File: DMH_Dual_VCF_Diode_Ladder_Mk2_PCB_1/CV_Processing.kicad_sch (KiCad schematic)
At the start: 45 parts, among them SW10 SW_DPDT_OnOn, SW7 SW_SPDT_OnOffOn, SW9 SW_SPDT_OnOffOn, U5 TL074, U6 TL074, U7 TL074

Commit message: Added CV3 and Drive CV to I/O pages
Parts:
- SW7, SW9: Function Bus CV Amt -> CV 3 Amt
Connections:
- net Bus CV A Input renamed CV3 A Input
- net Bus CV B Input renamed CV3 B Input
- net Link Switch renamed Link CV Switch
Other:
- moved on the sheet: D3, D4, D5, R11, R12, R13, R14, R15, RV6, SW10

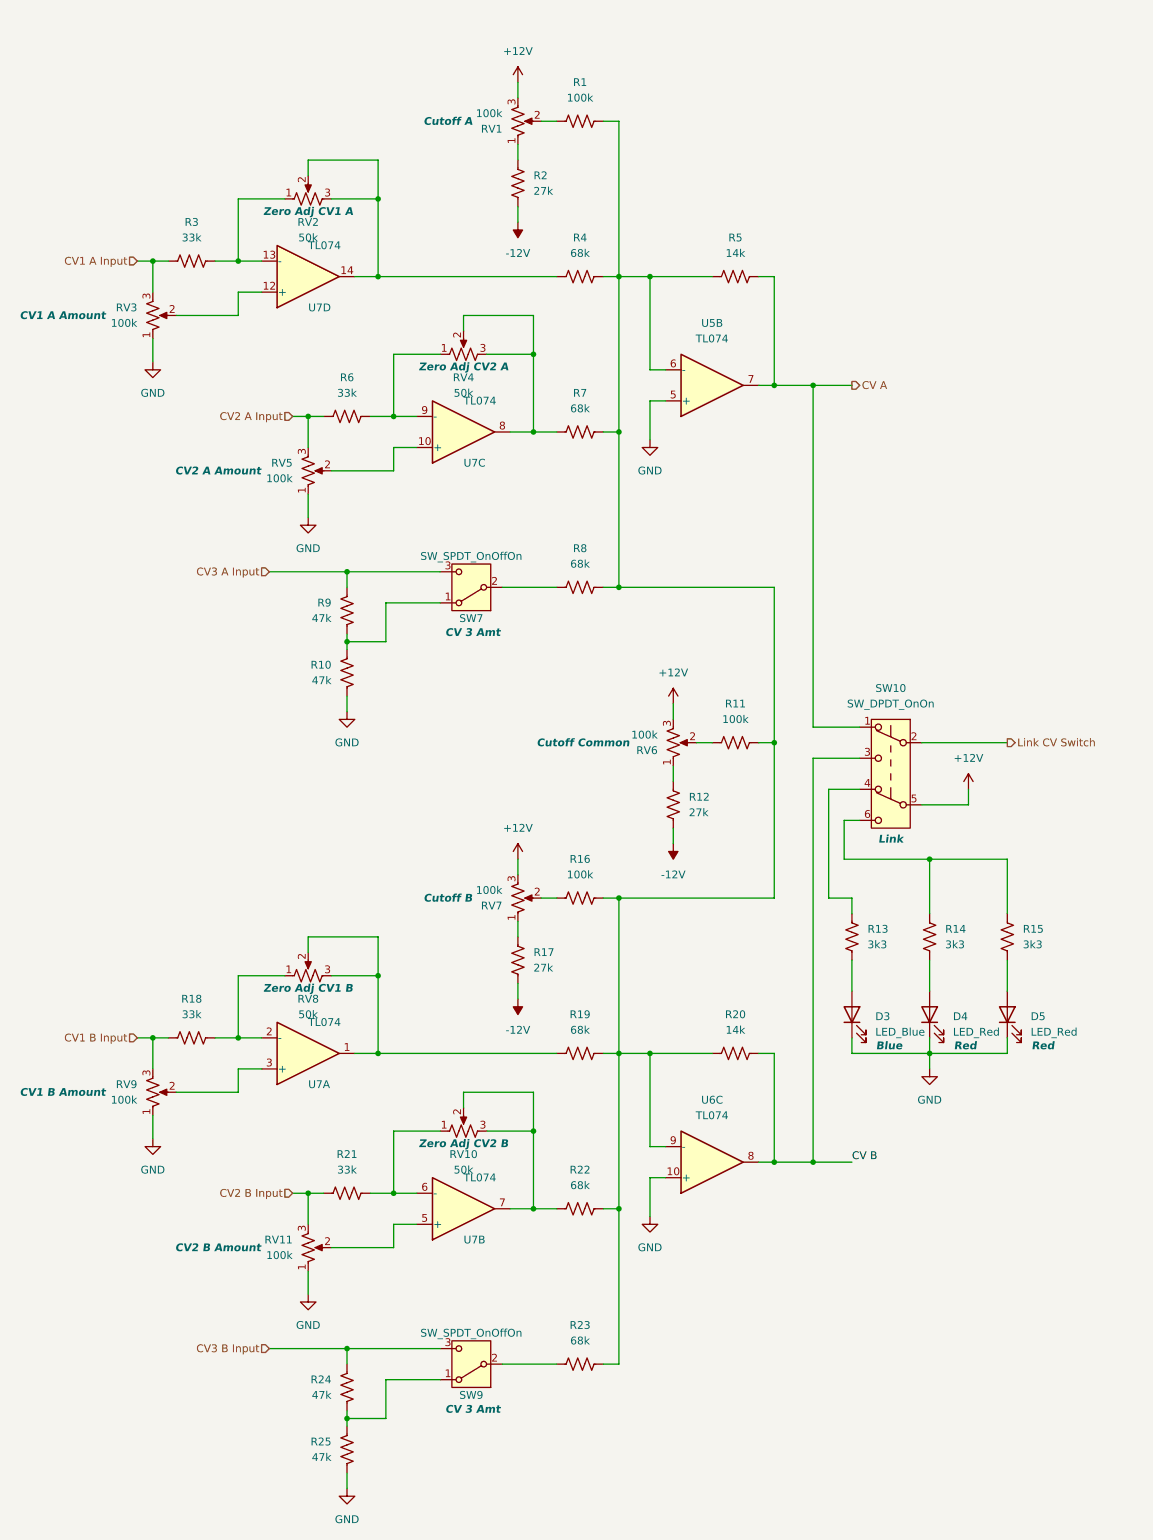
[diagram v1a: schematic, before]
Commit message: Added board-to-board pins to schematic
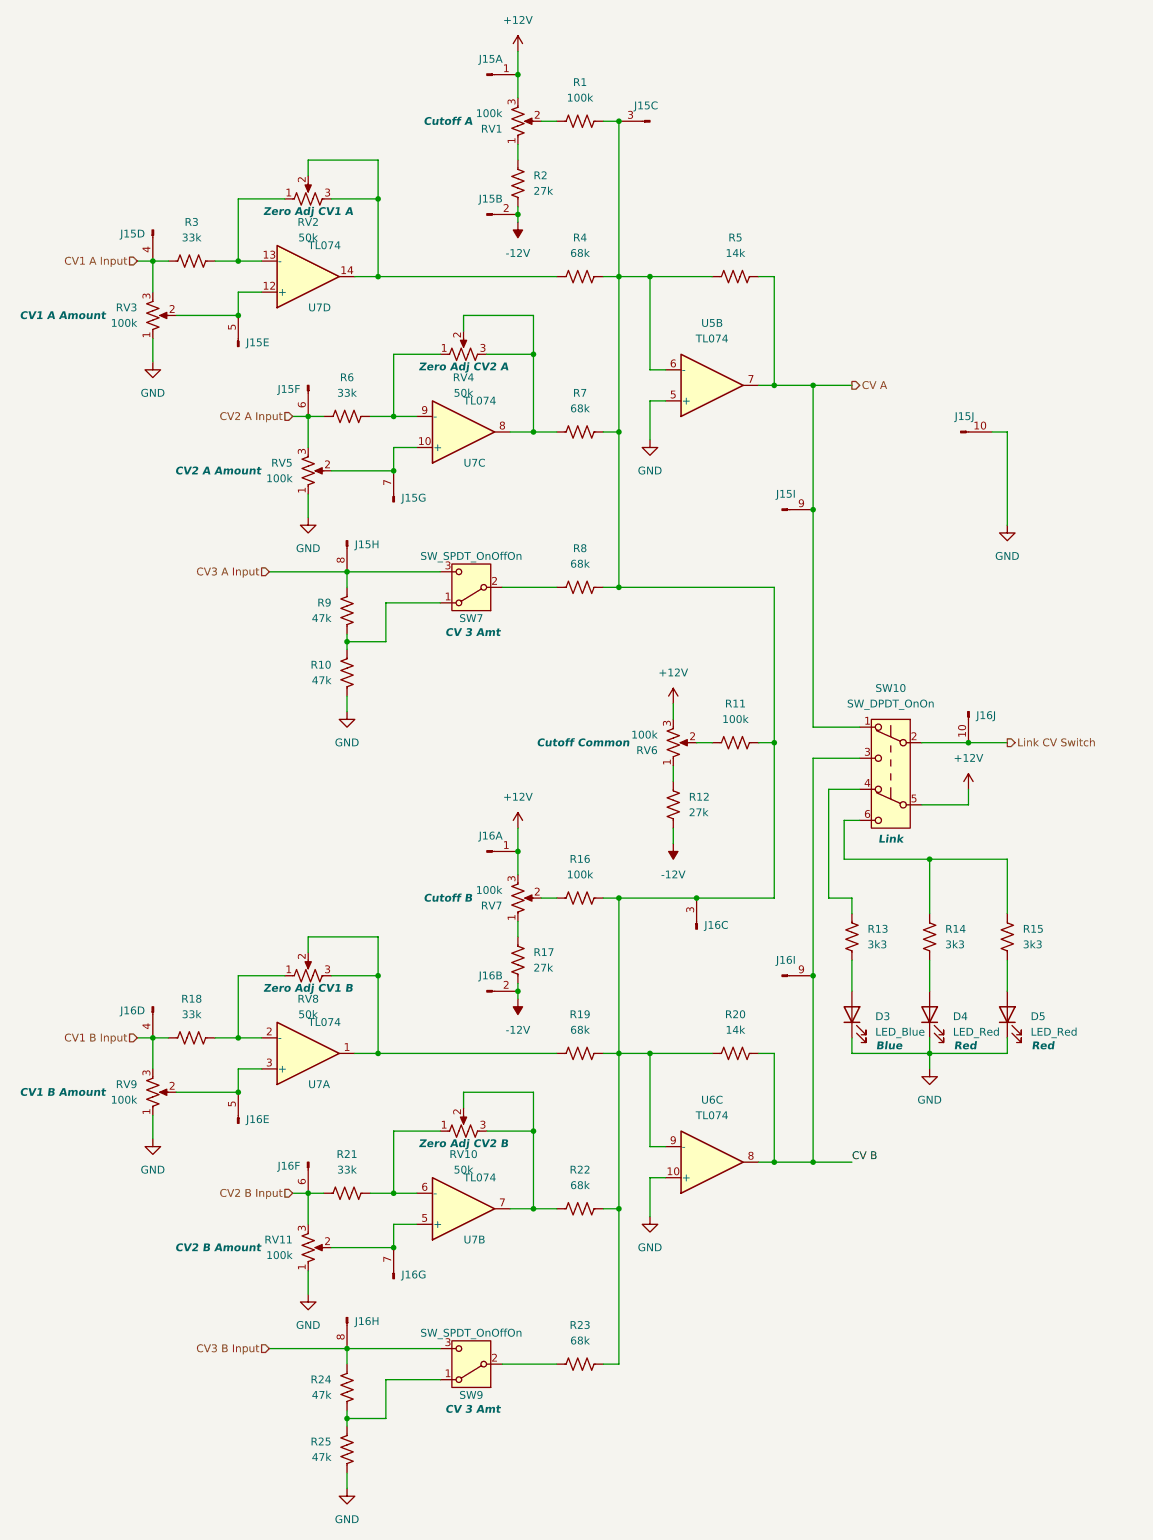
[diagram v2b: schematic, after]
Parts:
- added J15, J16: Conn_01x10_PinHeader, Connector_PinHeader_2.54mm:PinHeader_1x10_P2.54mm_Vertical, symbol SynthStuff:Conn_01x10_PinHeader
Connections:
- net +12V: now also J15.1 (Pin_1), J16.1 (Pin_1)
- net -12V: now also J15.2 (Pin_2), J16.2 (Pin_2)
- net CV A: now also J15.9 (Pin_9)
- net CV B: now also J16.9 (Pin_9)
- net CV1 A Input: now also J15.4 (Pin_4)
- net CV1 B Input: now also J16.4 (Pin_4)
- net CV2 A Input: now also J15.6 (Pin_6)
- net CV2 B Input: now also J16.6 (Pin_6)
- net CV3 A Input: now also J15.8 (Pin_8)
- net CV3 B Input: now also J16.8 (Pin_8)
- net GND: now also J15.10 (Pin_10)
- net Link CV Switch: now also J16.10 (Pin_10)
- net at R1.2, R11.2, R16.2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: now also J15.3 (Pin_3), J16.3 (Pin_3)
- net at RV11.2, U7.5 (+): now also J16.7 (Pin_7)
- net at RV3.2, U7.12 (+): now also J15.5 (Pin_5)
- net at RV5.2, U7.10 (+): now also J15.7 (Pin_7)
- net at RV9.2, U7.3 (+): now also J16.5 (Pin_5)

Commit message: Added inter-board pins to all circuits
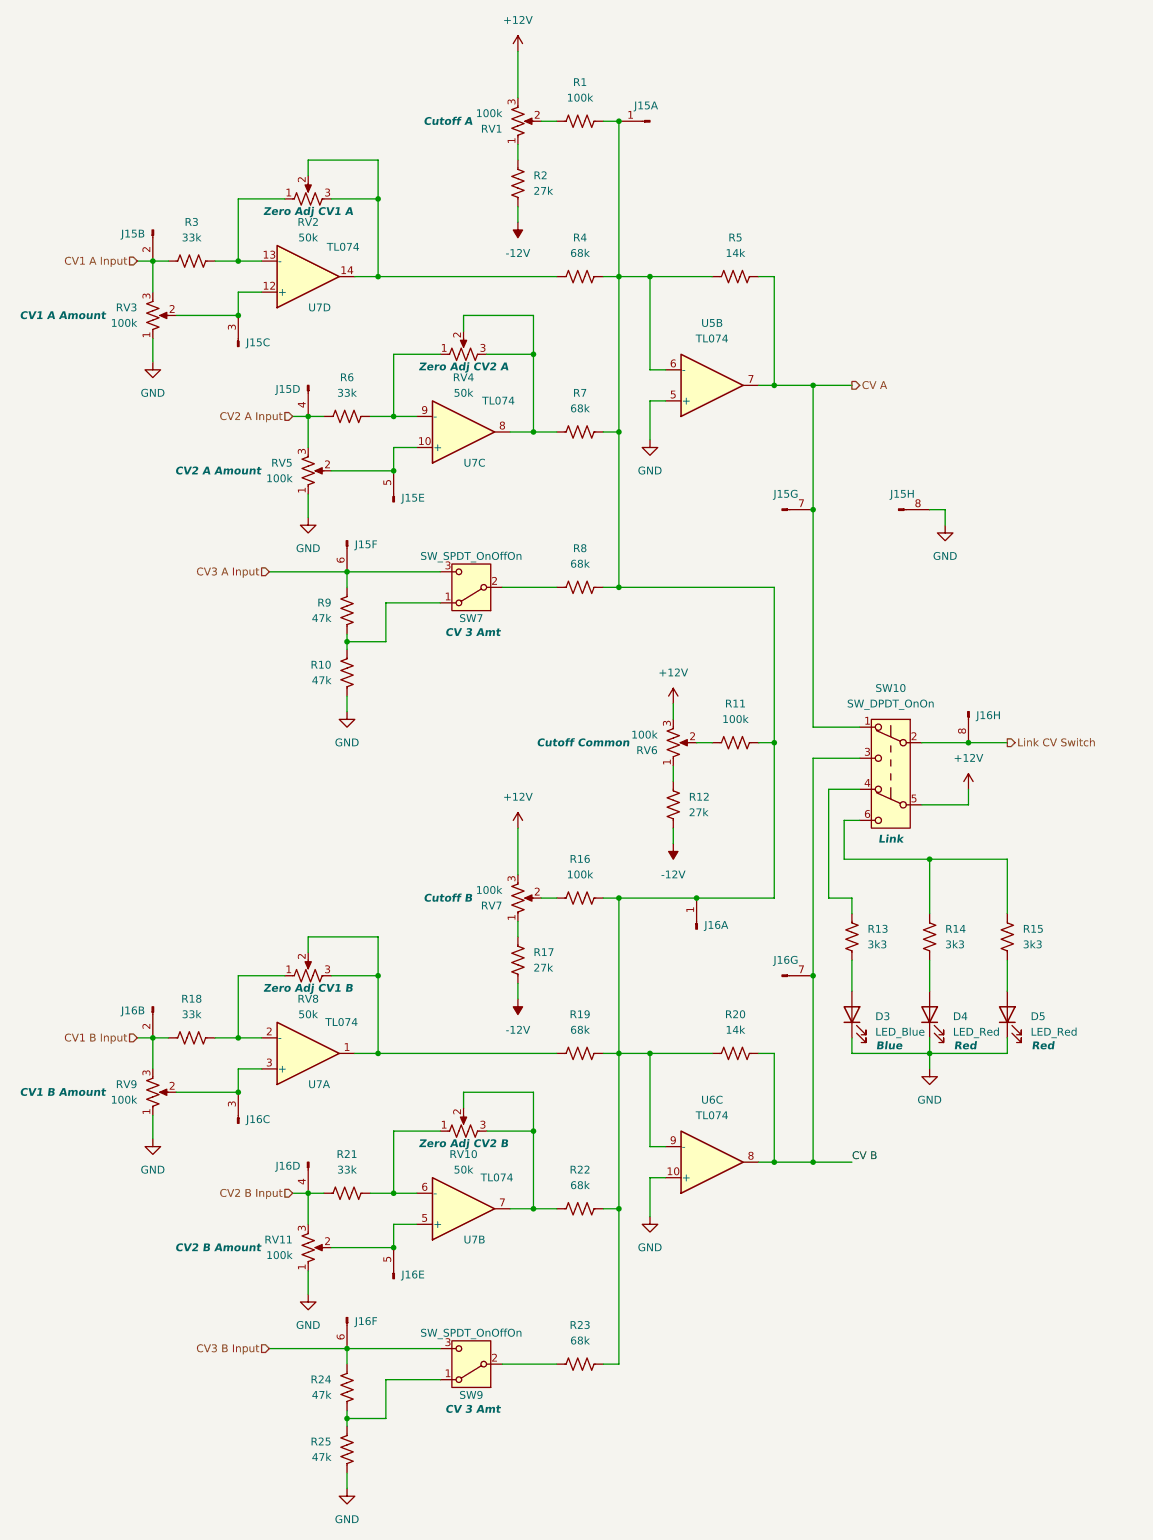
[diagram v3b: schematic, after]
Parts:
- removed unit 2 of J15
- removed unit 10 of J15
- removed unit 1 of J15
- removed unit 4 of J15
- removed unit 2 of J16
- removed unit 1 of J16
- added unit 8 of J15
- added unit 2 of J15
- J15, J16: value Conn_01x10_PinHeader -> Conn_01x08_PinHeader; symbol SynthStuff:Conn_01x10_PinHeader -> SynthStuff:Conn_01x08_PinHeader
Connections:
- net CV A: now also J15.7 (Pin_7); no longer J15.9 (Pin_9)
- net CV B: now also J16.7 (Pin_7); no longer J16.9 (Pin_9)
- net CV1 A Input: now also J15.2 (Pin_2)
- net CV1 B Input: now also J16.2 (Pin_2); no longer J16.4 (Pin_4)
- net CV2 A Input: now also J15.4 (Pin_4); no longer J15.6 (Pin_6)
- net CV2 B Input: now also J16.4 (Pin_4); no longer J16.6 (Pin_6)
- net CV3 A Input: now also J15.6 (Pin_6); no longer J15.8 (Pin_8)
- net CV3 B Input: now also J16.6 (Pin_6); no longer J16.8 (Pin_8)
- net GND: now also J15.8 (Pin_8)
- net Link CV Switch: now also J16.8 (Pin_8); no longer J16.10 (Pin_10)
- net at R1.2, R11.2, R16.2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: now also J15.1 (Pin_1), J16.1 (Pin_1); no longer J15.3 (Pin_3), J16.3 (Pin_3)
- net at RV11.2, U7.5 (+): now also J16.5 (Pin_5); no longer J16.7 (Pin_7)
- net at RV9.2, U7.3 (+): now also J16.3 (Pin_3); no longer J16.5 (Pin_5)
- net at RV3.2, U7.12 (+): now also J15.3 (Pin_3); no longer J15.5 (Pin_5)
- net at RV5.2, U7.10 (+): now also J15.5 (Pin_5); no longer J15.7 (Pin_7)

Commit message: Connecting main blocks in progress
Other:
- company: (none) -> DMH Instruments
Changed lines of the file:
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@@
 	(paper "A4" portrait)
 	(title_block
-		(comment 1 "PCB for 10cm Kosmo format synthesizer module")
+		(company "DMH Instruments")
+		(comment 1 "PCB for 15cm Kosmo format synthesizer module")
 	)
 	(junction

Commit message: Reannotated OpAmps and cleared errors
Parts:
- renumbered U5 to U7, U6 to U8, U7 to U8
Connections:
- net CV A: now also U7.1; no longer U7.7
- net CV B: now also U8.14; no longer U8.8
- net GND: now also U7.3 (+), U8.12 (+); no longer U7.5 (+), U8.10 (+)
- net at J15.1 (Pin_1), J16.1 (Pin_1), R1.2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: now also U7.2 (-), U8.13 (-); no longer U7.6 (-), U8.9 (-)
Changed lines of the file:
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@@
 		(at 129.54 208.28 0)
 		(mirror x)
-		(unit 3)
+		(unit 4)
 		(exclude_from_sim no)
 		(in_bom yes)
@@
 		(dnp no)
 		(fields_autoplaced yes)
-		(property "Reference" "U6"
+		(property "Reference" "U8"
 			(at 129.54 198.12 0)
 			(effects
@@
 			(project "DMH_Dual_VCF_Diode_Ladder_PCB"
 				(path "/58f4306d-5387-4983-bb08-41a2313fd315/ec2d44bc-ed06-4f0b-a22e-df640fa5e089"
-					(reference "U6")
-					(unit 3)
+					(reference "U8")
+					(unit 4)
 				)
 			)
@@
 		(on_board yes)
 		(dnp no)
-		(property "Reference" "U7"
+		(property "Reference" "U8"
 			(at 63.5 195.58 0)
 			(effects
@@
 			(project "DMH_Dual_VCF_Diode_Ladder_PCB"
 				(path "/58f4306d-5387-4983-bb08-41a2313fd315/ec2d44bc-ed06-4f0b-a22e-df640fa5e089"
-					(reference "U7")
+					(reference "U8")
 					(unit 1)
 				)
@@
 		(at 129.54 81.28 0)
 		(mirror x)
-		(unit 2)
+		(unit 1)
 		(exclude_from_sim no)
 		(in_bom yes)
@@
 		(dnp no)
 		(fields_autoplaced yes)
-		(property "Reference" "U5"
+		(property "Reference" "U7"
 			(at 129.54 71.12 0)
 			(effects
@@
 			(project "DMH_Dual_VCF_Diode_Ladder_PCB"
 				(path "/58f4306d-5387-4983-bb08-41a2313fd315/ec2d44bc-ed06-4f0b-a22e-df640fa5e089"
-					(reference "U5")
-					(unit 2)
+					(reference "U7")
+					(unit 1)
 				)
 			)
@@
 		(on_board yes)
 		(dnp no)
-		(property "Reference" "U7"
+		(property "Reference" "U8"
 			(at 88.9 220.98 0)
 			(effects
@@
 			(project "DMH_Dual_VCF_Diode_Ladder_PCB"
 				(path "/58f4306d-5387-4983-bb08-41a2313fd315/ec2d44bc-ed06-4f0b-a22e-df640fa5e089"
-					(reference "U7")
+					(reference "U8")
 					(unit 2)
 				)
